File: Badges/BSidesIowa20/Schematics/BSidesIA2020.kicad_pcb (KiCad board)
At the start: 2 copper layers, 76.9 x 133.3 mm, 3 parts

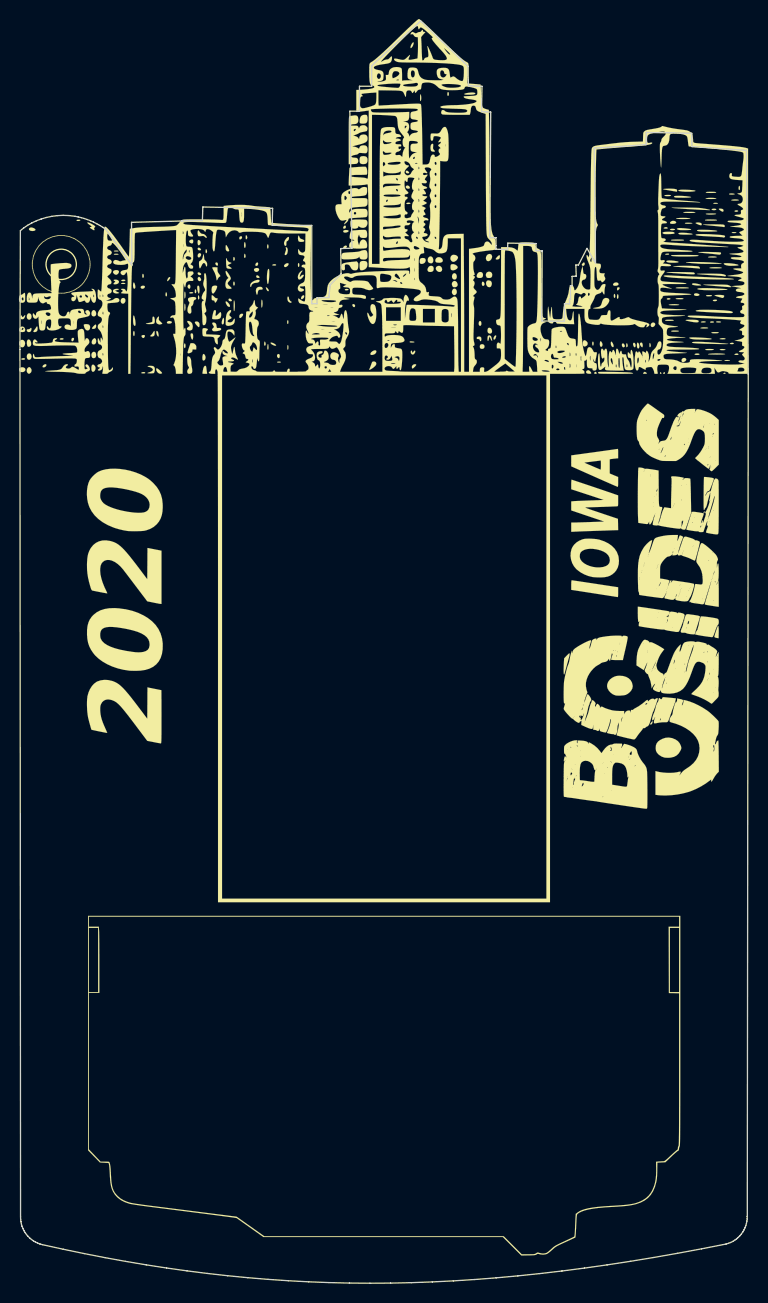
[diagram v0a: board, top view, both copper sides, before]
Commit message: FJE Badge Charlieplexing done
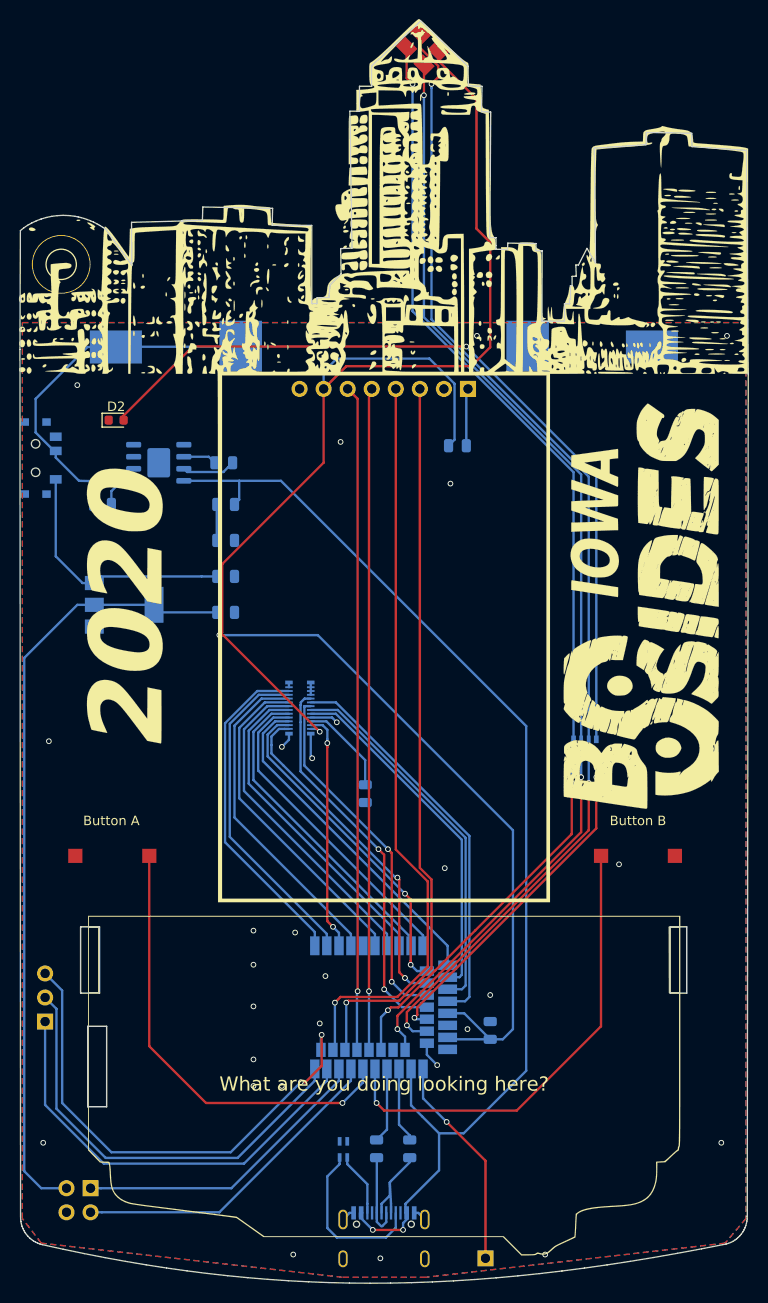
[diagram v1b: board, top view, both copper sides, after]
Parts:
- added BT1: Battery_Cell, Tests:Dongguan14500, B.Cu at (145.8, 61.8)
- added Button A: SW_DIP_x01, Dragos:1TS002E-2500-2500-CT-HYP-Button, F.Cu at (117.1, 115.5)
- added Button B: SW_DIP_x01, Dragos:1TS002E-2500-2500-CT-HYP-Button, F.Cu at (172.6, 115.5)
- added C1: 4.7uF, Capacitor_SMD:C_0805_2012Metric, B.Cu at (157.0, 133.9)
- added C14: 10uF, Capacitor_SMD:C_0805_2012Metric, B.Cu at (129.1, 78.4)
- added C17: 10uF, Capacitor_SMD:C_0805_2012Metric, B.Cu at (116.1, 78.4)
- added C2: 1uF, Capacitor_SMD:C_0805_2012Metric, B.Cu at (129.1, 86.0)
- added C3: 1uF, Capacitor_SMD:C_0805_2012Metric, B.Cu at (129.1, 89.8)
- added D1: LED_BGRA, Dragos:EKINGLUX-E6, F.Cu at (149.8, 30.3)
- added D2: LED, LED_SMD:LED_0603_1608Metric, F.Cu at (117.5, 69.5)
- added J1: Conn_02x02_Odd_Even, Connector_PinHeader_2.54mm:PinHeader_2x02_P2.54mm_Vertical, B.Cu at (114.8, 150.6)
- added J2: Conn_01x01, Connector_PinHeader_2.54mm:PinHeader_1x01_P2.54mm_Vertical, B.Cu at (156.5, 158.0)
- added J3: Conn_01x03, Connector_PinHeader_2.54mm:PinHeader_1x03_P2.54mm_Vertical, B.Cu at (110.0, 133.0)
- added J4: Conn_01x08, Connector_PinHeader_2.54mm:PinHeader_1x08_P2.54mm_Vertical, B.Cu at (154.7, 66.2)
- added J7: USB_C_Receptacle, Tests:USB_C_Receptical-Jing, B.Cu at (145.8, 153.9)
- added L1: L_Small, Inductor_SMD:L_0805_2012Metric, B.Cu at (143.8, 108.9)
- added Power->: SW3, BreadBoardPwr:SK-3296S_switch, B.Cu at (109.0, 73.5)
- added R1: 27Ohm, Resistor_SMD:R_0805_2012Metric, B.Cu at (148.5, 146.4)
- added R2: 1k, Resistor_SMD:R_0805_2012Metric, B.Cu at (128.9, 74.0)
- added R3: 27Ohm, Resistor_SMD:R_0805_2012Metric, B.Cu at (145.0, 146.4)
- added R4: R_Small, Resistor_SMD:R_0805_2012Metric, B.Cu at (153.5, 72.2)
- added R5: 1.5, Resistor_SMD:R_0805_2012Metric, B.Cu at (129.1, 82.2)
- added RN1: 10k, Resistor_SMD:R_Array_Concave_2x0603, B.Cu at (141.5, 146.5)
- added RN3: 270, Resistor_SMD:R_Array_Convex_4x0603, B.Cu at (167.0, 104.1)
- added U1: E73-2G4M08S1C, E73:E73-2G4M08S1C, B.Cu at (142.5, 131.0)
- added U2: TLV1117-33, Package_TO_SOT_SMD:SOT-223-3_TabPin2, B.Cu at (118.3, 89.0)
- added U3: HX4056, Package_SO:HSOP-8-1EP_3.9x4.9mm_P1.27mm_EP2.41x3.1mm, B.Cu at (122.0, 74.0)
- added U4: BBQ10KBD, Connectors_Hirose_extra:BM14B(0.8)-24DS-0.4V(53), B.Cu at (136.9, 99.9)
- moved G*** 228.4 mm to (164.0, 159.0)
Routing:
- net VCC: track 0.00 -> 282.1 mm, vias 0 -> 2
- net +5V: track 0.00 -> 123.9 mm, vias 0 -> 2
- net Net-(D2-Pad2): track 0.00 -> 86.8 mm, vias 0 -> 1
- net Net-(D1-Pad3): track 0.00 -> 82.5 mm, vias 0 -> 1
- net Net-(D1-Pad1): track 0.00 -> 80.4 mm, vias 0 -> 1
- net RST: track 0.00 -> 78.8 mm, vias 0 -> 1
- net Net-(D1-Pad2): track 0.00 -> 78.1 mm, vias 0 -> 1
- net DC: track 0.00 -> 77.2 mm, vias 0 -> 1
- net SCL: track 0.00 -> 70.3 mm, vias 0 -> 1
- net SDA: track 0.00 -> 69.9 mm, vias 0 -> 1
- net Net-(J3-Pad3): track 0.00 -> 52.7 mm, vias 0 -> 2
- net ButtonB: track 0.00 -> 49.4 mm, vias 0 -> 1
- net ButtonA: track 0.00 -> 47.5 mm, vias 0 -> 1
- net Net-(J3-Pad2): track 0.00 -> 46.3 mm
- net Net-(J3-Pad1): track 0.00 -> 46.0 mm
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- added copper zone on B.Cu, net VSS
- added copper zone on F.Cu, net VSS
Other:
- outline, holes or cut-outs redrawn
- net class Default: clearance 0.2 -> 0.15
- rule pad_to_mask_clearance: 0.2 -> 0.15
- rule trace_clearance: 0.2 -> 0.15
- board text added: "+ -"
- board text added: "@RMA_Electronics"
- board text added: "P1.06 P0.10 P0.09"
- board text added: "Replacing it with with one may cause a small explosion"
- board text added: "SWDIO SWCLK"
- board text added: "THIS IS NOT A AA BATTERY"
- board text added: "What are you doing looking here?"
